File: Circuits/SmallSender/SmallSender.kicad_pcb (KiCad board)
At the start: 2 copper layers, 28 x 49.6 mm, 17 parts, among them P1 WRITER-VCC, Q1 RUE002N02, SW1 JB-15FBP2, SW2 MKA-10110, U1 TWE_LITE_SMD, U2 HN2S01FU, U3 TCM809RVNB

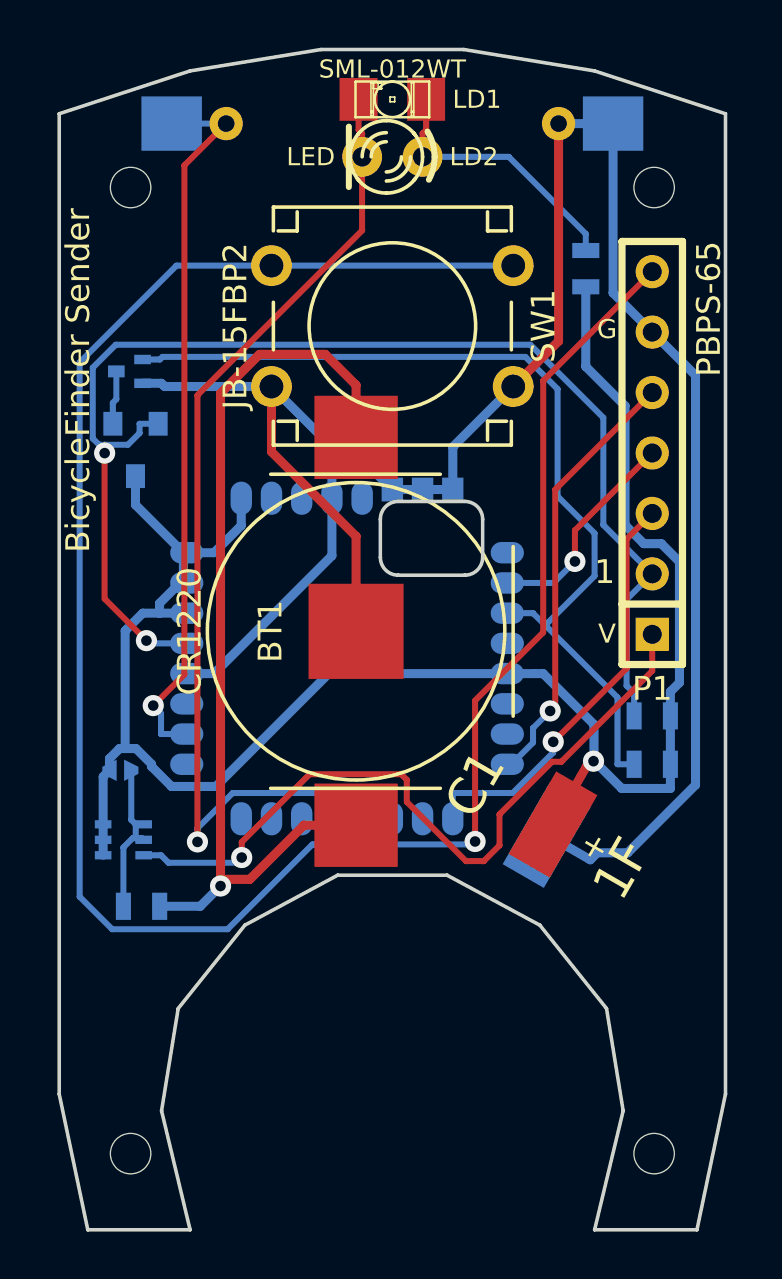
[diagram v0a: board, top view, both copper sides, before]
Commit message: Relocated the reset monitor.
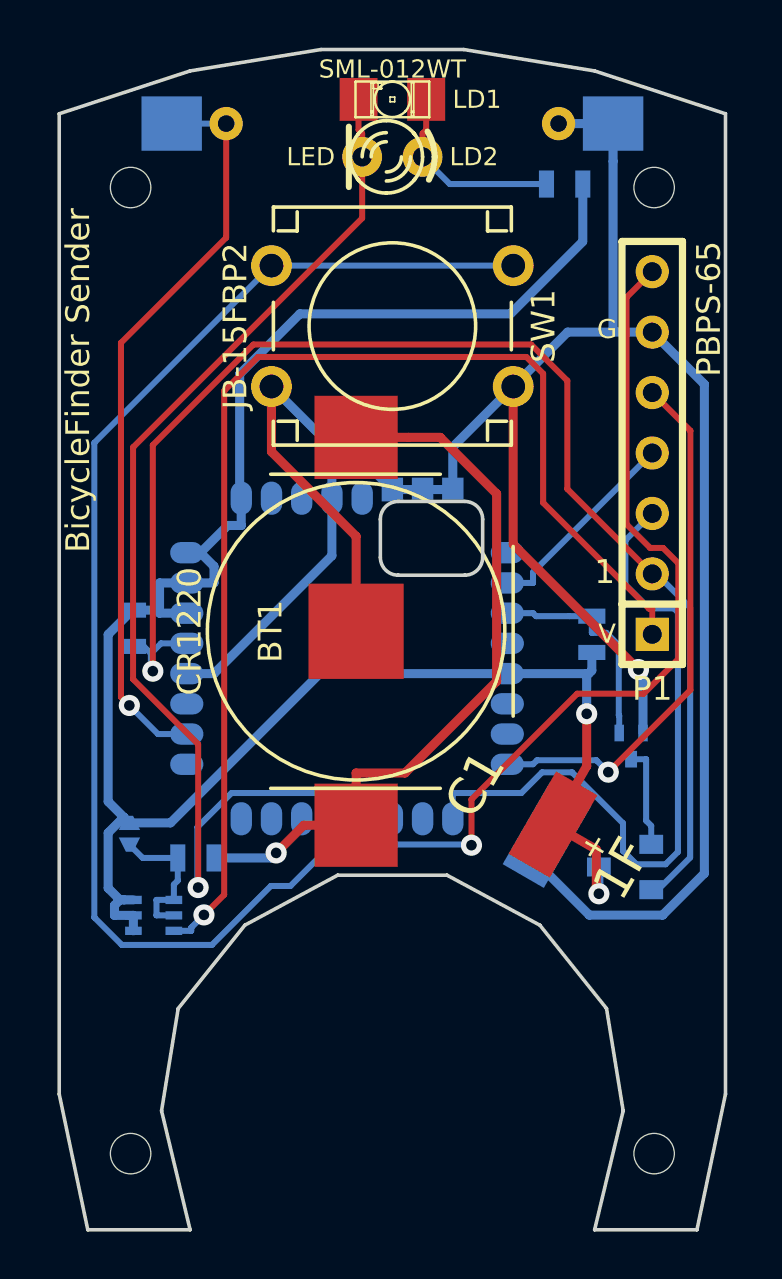
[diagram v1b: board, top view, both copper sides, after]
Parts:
- moved U3 27.0 mm to (36.2, 48.0), turned to 270 degrees
- moved Q1 26.3 mm to (36.4, 42.9), turned to 0 degrees
- moved R4 22.2 mm to (15.5, 38.0), turned to 270 degrees
- moved R3 6.02 mm to (34.8, 38.2), turned to 90 degrees
- moved R2 3.67 mm to (33.7, 19.3), turned to 180 degrees
- moved U2 3.42 mm to (16.4, 50.0)
- moved R1 3.06 mm to (18.2, 47.6)
- moved JP1 2.69 mm to (15.4, 46.6), turned to 90 degrees
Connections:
- net /3V3 renamed /ExVcc
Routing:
- net /DO1: track 39.1 -> 9.35 mm
- net /ExVcc: track 31.1 -> 51.2 mm
- net /RXD: track 17.8 -> 29.6 mm, vias 1 -> 0
- net GND: track 95.5 -> 106.8 mm, vias 0 -> 1
- net /3V: track 39.4 -> 31.0 mm
- net /Vcc: track 79.2 -> 86.9 mm, vias 1 -> 2
- net /DO4: track 44.6 -> 50.7 mm
- net /TXD: track 18.2 -> 22.6 mm
- net /CFG: track 32.9 -> 36.7 mm
- net /LED: track 11.4 -> 8.16 mm
- net /RST: track 54.2 -> 57.1 mm, vias 2 -> 1
- net /DI1: track 56.1 -> 53.9 mm
- net /QGND: track 2.26 -> 4.30 mm
- net /DI4: track 30.4 -> 31.6 mm
- net /CHG: track 6.78 -> 6.21 mm
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
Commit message: Omit external pull-up registers.
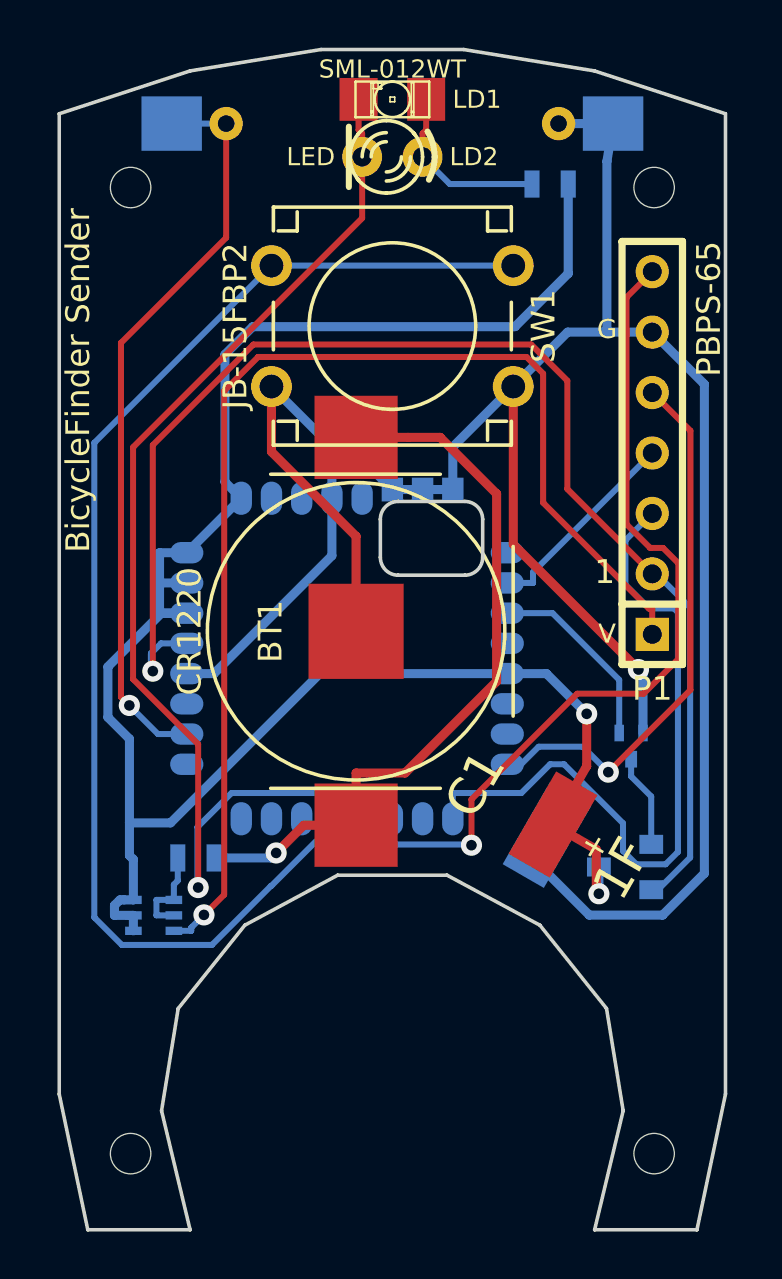
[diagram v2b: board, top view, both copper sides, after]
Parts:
- removed JP1: BYPASS, JUMPER
- removed R3, R4: 10M, SM0603_Resistor
- R2: value 680 -> 1k
- moved R2 0.61 mm to (33.0, 19.3)
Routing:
- net /CHG: track 6.21 -> 3.94 mm
- net /Vcc: track 86.9 -> 85.0 mm
- net /DO1: track 9.35 -> 8.10 mm
- net /RST: track 57.1 -> 56.2 mm
- net /LED: track 8.16 -> 7.55 mm

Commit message: Replaced tactical switch to SMD type.
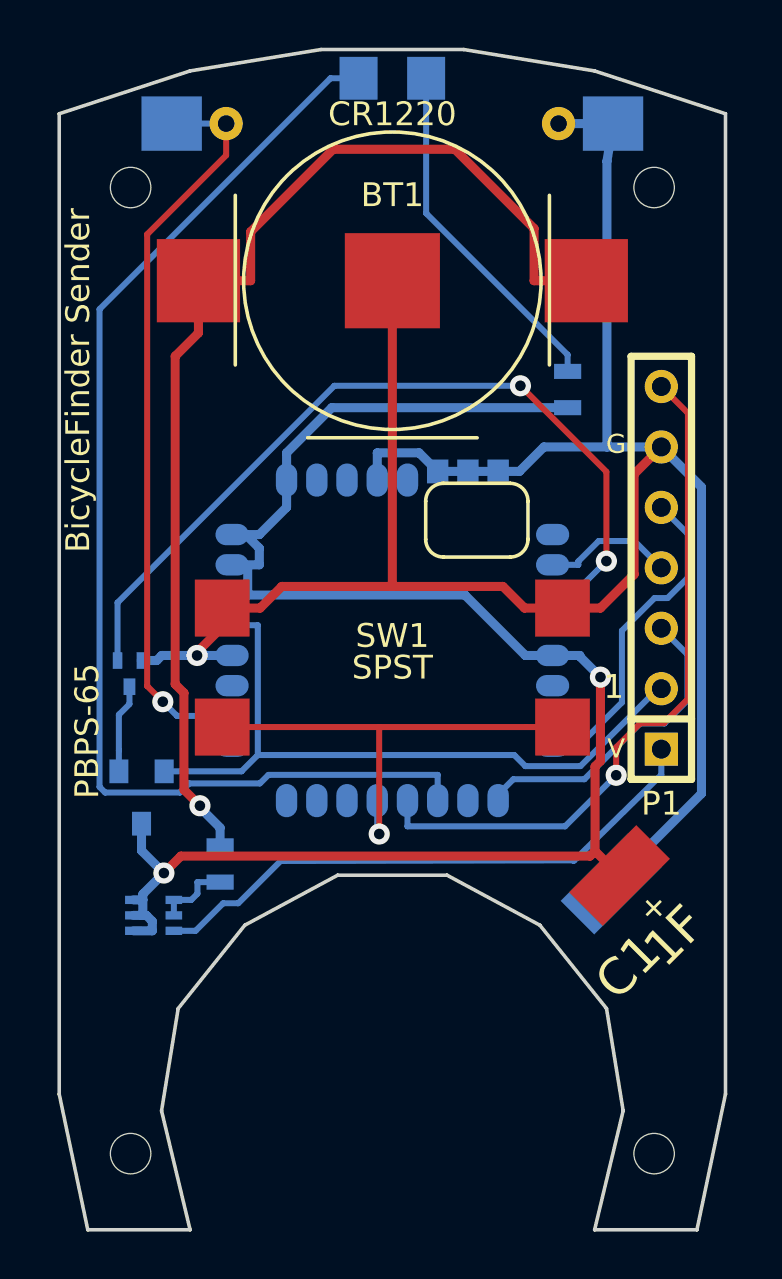
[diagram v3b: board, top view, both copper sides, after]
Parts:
- removed LD2: LED, LED-3MM
- LD1: moved to B.Cu
- SW1: value JB-15FBP2 -> SPST; footprint JB-15HFBP2 -> B3FS-4002P
- U1: footprint TWE-001L-NC7 -> TWE-001L-SMD-noNTH
- moved Q1 21.3 mm to (15.4, 39.9)
- moved U3 20.5 mm to (15.9, 45.1), turned to 0 degrees
- moved BT1 14.8 mm to (26.4, 23.4), turned to 0 degrees
- moved SW1 14.4 mm to (26.4, 39.6), turned to 0 degrees
- moved R2 8.67 mm to (33.8, 27.9), turned to 90 degrees
- moved P1 4.84 mm to (37.7, 35.4)
- moved U1 2.05 mm to (26.4, 38.5)
- moved R1 1.05 mm to (19.2, 47.9), turned to 270 degrees
- moved LD1 0.89 mm to (26.4, 14.9)
- turned C1 to 45 degrees
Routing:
- net /DI1: track 53.5 -> 20.2 mm, vias 0 -> 1
- net /RST: track 56.2 -> 29.3 mm, vias 1 -> 0
- net /ExVcc: track 51.2 -> 24.3 mm, vias 1 -> 0
- net /DO1: track 8.10 -> 35.0 mm, vias 0 -> 2
- net /3V: track 31.0 -> 48.3 mm
- net /RXD: track 29.9 -> 13.3 mm
- net GND: track 106.9 -> 94.4 mm
- net /Vcc: track 85.0 -> 73.0 mm
- net /TXD: track 23.0 -> 13.8 mm, vias 1 -> 0
- net /CFG: track 36.7 -> 29.4 mm
- net /LED: track 7.55 -> 14.8 mm
- net /PRG: track 8.62 -> 5.53 mm
- net /CHG: track 3.94 -> 3.19 mm
- net /DO4: vias 1 -> 0

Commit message: Switch GND by a voltage detector.
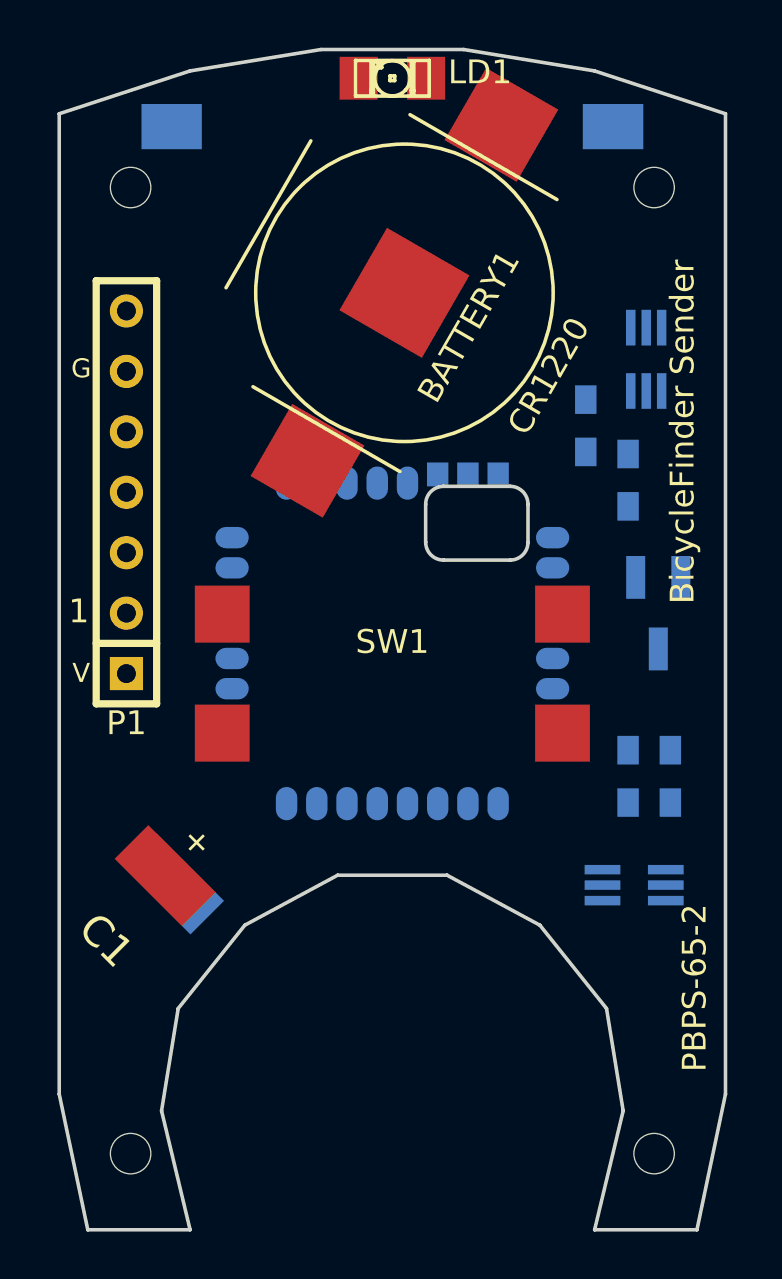
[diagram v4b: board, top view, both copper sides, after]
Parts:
- removed BT1: CR1220, BK-885
- removed PBPS-65: BicycleFinder Sender, PBPS-65+EDLC
- removed Q1: RUE002N02, EMT3
- added BATTERY1: CR1220, favorites:BK-885, F.Cu at (26.9, 23.9)
- added PBPS-65-2: BicycleFinder Sender, PBPS-65+EDLC, F.Cu at (26.4, 39.8)
- added R3: 10M, Resistors_SMD:R_0603_HandSoldering, B.Cu at (36.3, 31.8)
- added R4: 10M, Resistors_SMD:R_0603_HandSoldering, B.Cu at (38.1, 44.2)
- added U4: 2N7002DW, Housings_SOT-23_SOT-143_TSOT-6:SC-70-6_Handsoldering, B.Cu at (37.1, 26.7)
- C1: footprint SE-5R5-D105VYV -> favorites:SE-5R5-D105VYV
- LD1: footprint LED-1206 -> LEDs:LED-1206; moved to F.Cu
- P1: footprint WRITE-7P -> favorites:WRITE-7P
- R1: value 330 -> 1k; footprint SM0603_Resistor -> Resistors_SMD:R_0603_HandSoldering
- R2: footprint SM0603_Resistor -> Resistors_SMD:R_0603_HandSoldering
- SW1: footprint B3FS-4002P -> favorites:B3FS-4002P
- SW2: value MKA-10110 -> FR2S1015; footprint REEDSW -> favorites:FR2S1015
- U1: footprint TWE-001L-SMD-noNTH -> favorites:TWE-001L-SMD
- U2: footprint HN2S01FU -> Housings_SOT-23_SOT-143_TSOT-6:SC-70-6_Handsoldering
- U3: footprint SOT23 -> Housings_SOT-23_SOT-143_TSOT-6:SOT-23_Handsoldering
- moved U3 23.1 mm to (37.6, 37.3)
- moved P1 22.7 mm to (15.2, 32.3)
- moved U2 20.2 mm to (36.6, 48.8), turned to 270 degrees
- moved R1 17.5 mm to (36.3, 44.2)
- moved R2 1.70 mm to (34.5, 29.5)
- moved SW1 0.25 mm to (26.4, 39.9)
- moved SW2 0.13 mm to (26.4, 16.9)
- moved U1 0.13 mm to (26.4, 38.6)
- turned C1 to 135 degrees
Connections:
- SW1 pad 2: GND -> /TWE_GND
- SW2 pad 2: GND -> /TWE_GND
- U1 pad 1: (no net) -> Net-(U1-Pad1)
- U1 pad 10: (no net) -> Net-(U1-Pad10)
- U1 pad 14: (no net) -> Net-(U1-Pad14)
- U1 pad 15: (no net) -> Net-(U1-Pad15)
- U1 pad 16: (no net) -> Net-(U1-Pad16)
- U1 pad 17: (no net) -> Net-(U1-Pad17)
- U1 pad 19: (no net) -> Net-(U1-Pad19)
- U1 pad 20: GND -> /TWE_GND
- U1 pad 26: (no net) -> Net-(U1-Pad26)
- U1 pad 27: (no net) -> Net-(U1-Pad27)
- U1 pad 28: GND -> /TWE_GND
- U1 pad 29: (no net) -> Net-(U1-Pad29)
- U1 pad 30: GND -> /TWE_GND
- U1 pad 31: GND -> /TWE_GND
- U1 pad 32: GND -> /TWE_GND
- U1 pad 4: (no net) -> Net-(U1-Pad4)
- U1 pad 6: (no net) -> Net-(U1-Pad6)
- U1 pad 7: (no net) -> Net-(U1-Pad7)
- U3 pad 1: /QGND -> /TCM_GND
- U3 pad 2: /RST -> /RESET#
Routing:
- net GND: track 94.4 -> 0.00 mm, vias 1 -> 0
- net /Vcc: track 73.0 -> 0.00 mm, vias 2 -> 0
- net /DO4: track 50.7 -> 0.00 mm
- net /3V: track 48.3 -> 0.00 mm, vias 1 -> 0
- net /DO1: track 35.0 -> 0.00 mm, vias 2 -> 0
- net /DI4: track 31.4 -> 0.00 mm, vias 1 -> 0
- net /CFG: track 29.4 -> 0.00 mm, vias 1 -> 0
- net /RST: track 29.3 -> 0.00 mm
- net /ExVcc: track 24.3 -> 0.00 mm
- net /DI1: track 20.2 -> 0.00 mm, vias 1 -> 0
- net /LED: track 14.8 -> 0.00 mm
- net /TXD: track 13.8 -> 0.00 mm
- net /RXD: track 13.3 -> 0.00 mm
- net /PRG: track 5.53 -> 0.00 mm
- net /QGND: track 3.74 -> 0.00 mm
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
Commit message: Moved LED to front side.
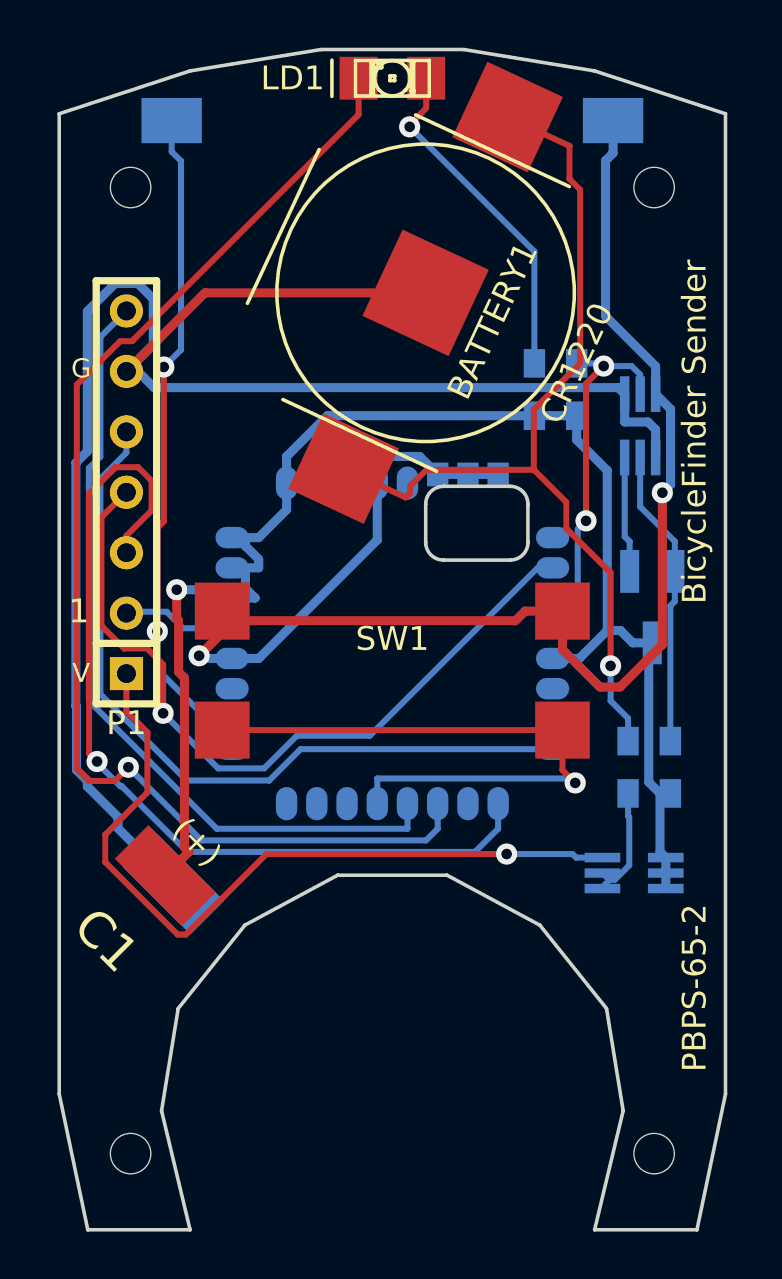
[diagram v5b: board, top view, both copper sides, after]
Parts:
- LD1: footprint LEDs:LED-1206 -> favorites:LED-1206
- U1: footprint favorites:TWE-001L-SMD -> favorites:TWE-001L-NC7
- moved R3 4.38 mm to (34.2, 27.9), turned to 90 degrees
- moved U4 2.81 mm to (36.8, 29.5)
- moved R2 2.64 mm to (32.4, 27.9)
- moved BATTERY1 0.89 mm to (27.8, 23.9), turned to 245 degrees
- moved U2 0.51 mm to (36.6, 48.3)
- moved R1 0.38 mm to (36.3, 43.8)
- moved R4 0.38 mm to (38.1, 43.8)
- moved U3 0.36 mm to (37.3, 37.1)
- moved SW2 0.25 mm to (26.4, 16.6)
- moved SW1 0.13 mm to (26.4, 39.8)
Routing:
- net GND: track 0.00 -> 71.9 mm
- net /TWE_GND: track 0.00 -> 65.9 mm, vias 0 -> 2
- net /Vcc: track 0.00 -> 63.6 mm, vias 0 -> 1
- net /DO4: track 0.00 -> 52.4 mm, vias 0 -> 1
- net /3V: track 0.00 -> 39.4 mm, vias 0 -> 1
- net /RXD: track 0.00 -> 38.1 mm, vias 0 -> 1
- net /CFG: track 0.00 -> 33.7 mm
- net /ExVcc: track 0.00 -> 32.6 mm, vias 0 -> 1
- net /TXD: track 0.00 -> 32.5 mm
- net /PRG: track 0.00 -> 32.2 mm, vias 0 -> 1
- net /DI4: track 0.00 -> 27.6 mm, vias 0 -> 2
- net /DI1: track 0.00 -> 26.2 mm, vias 0 -> 1
- net /DO1: track 0.00 -> 14.9 mm, vias 0 -> 2
- net /LED: track 0.00 -> 14.4 mm, vias 0 -> 1
- net /RESET#: track 0.00 -> 12.6 mm
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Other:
- net class Default: clearance 0.254 -> 0.229
- net class Power: clearance 0.254 -> 0.229
- rule trace_clearance: 0.254 -> 0.229
